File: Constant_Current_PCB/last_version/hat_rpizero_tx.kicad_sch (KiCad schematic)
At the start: 25 parts, among them SW1 MK-11C04-G013, SW2 Conn_01x04, U4 TLV75533PDBVR

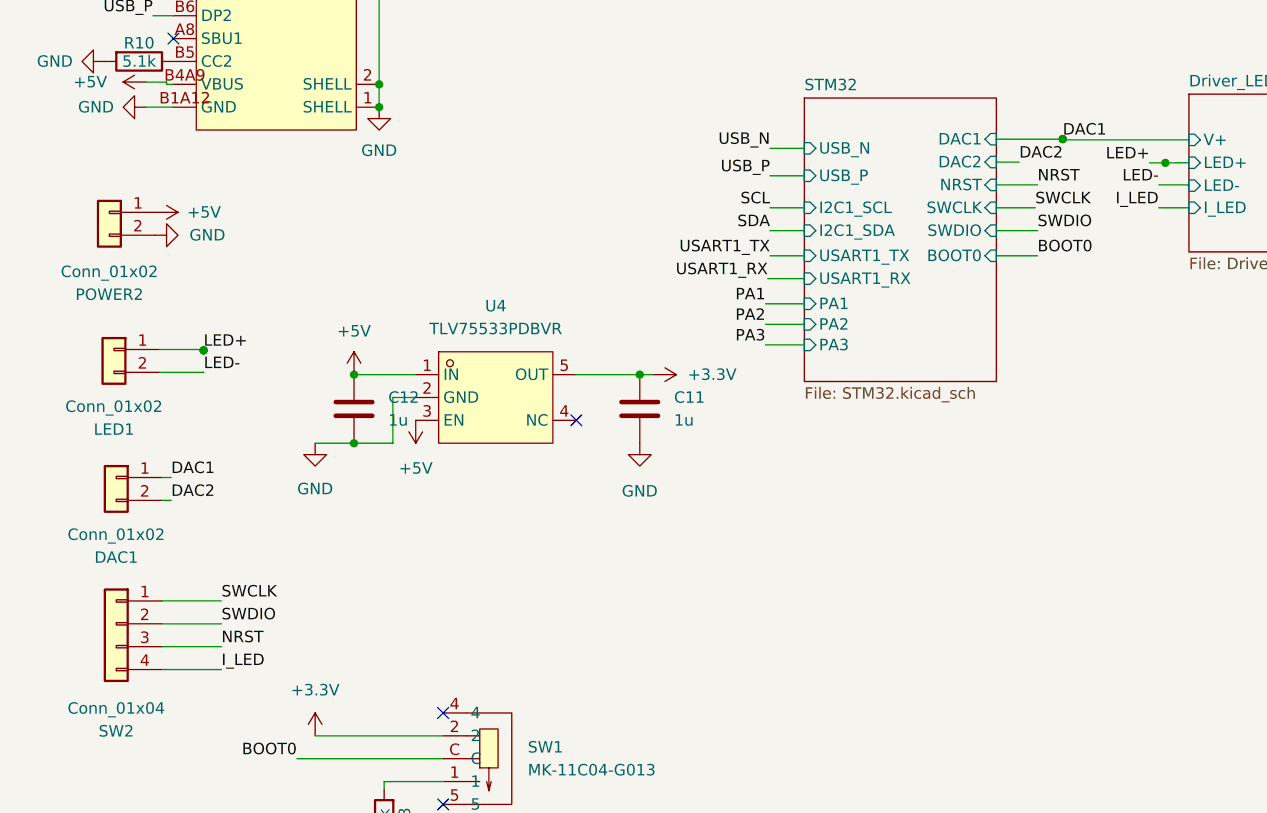
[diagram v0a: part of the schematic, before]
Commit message: fixed NRST
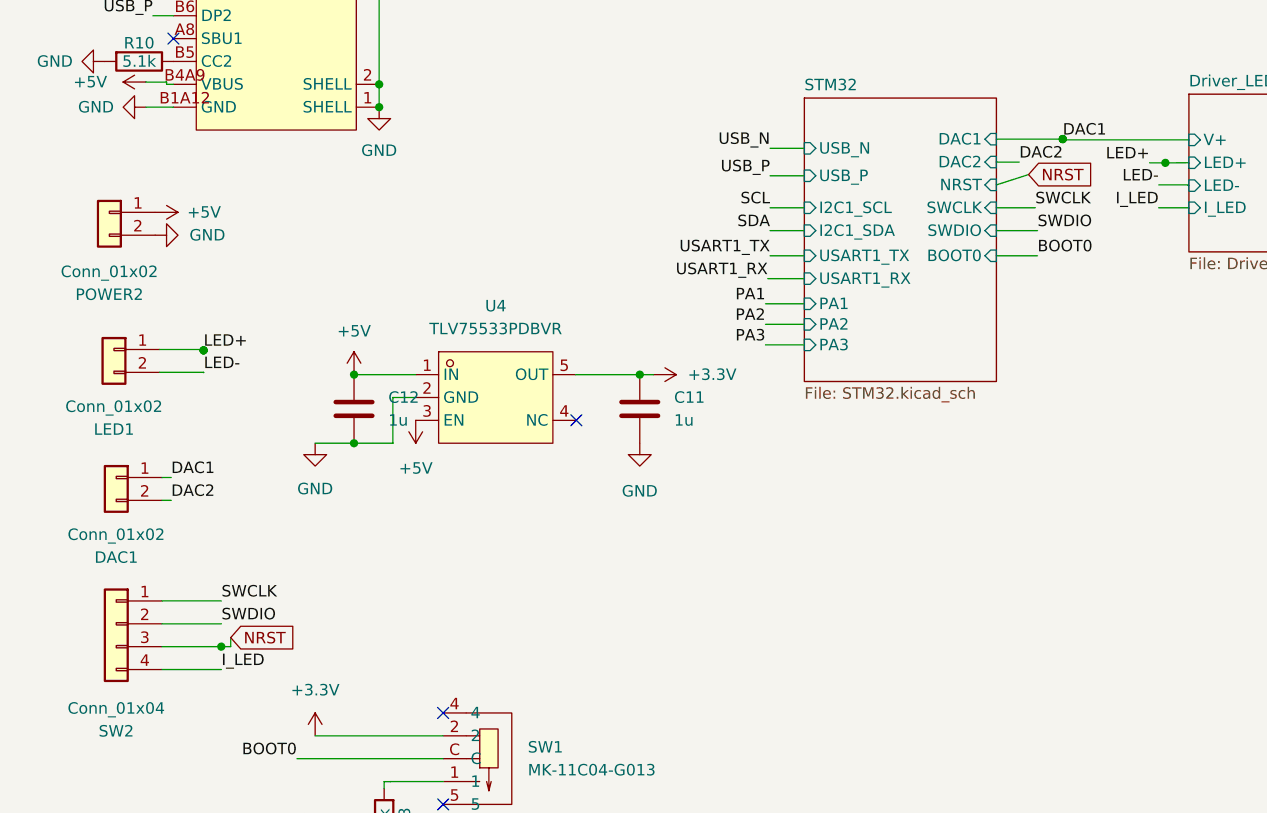
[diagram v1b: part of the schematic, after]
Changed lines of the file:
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@@
+	)
+	(junction
+		(at 36.05 111.5)
+		(diameter 0)
+		(color 0 0 0 0)
 	)
 	(junction
@@
 	(wire
 		(pts
+			(xy 37.1 110.5) (xy 37.1 111.5)
+		)
+		(stroke
+			(width 0)
+			(type default)
+		)
+	)
+	(wire
+		(pts
 			(xy 96.774 70.612) (xy 100.838 70.612)
 		)
@@
 	(wire
 		(pts
+			(xy 36.05 111.5) (xy 29.464 111.506)
+		)
+		(stroke
+			(width 0)
+			(type default)
+		)
+	)
+	(wire
+		(pts
+			(xy 125.75 59.05) (xy 122.174 60.198)
+		)
+		(stroke
+			(width 0)
+			(type default)
+		)
+	)
+	(wire
+		(pts
 			(xy 53.594 23.622) (xy 53.594 26.162)
 		)
@@
 	(wire
 		(pts
-			(xy 36.068 111.506) (xy 29.464 111.506)
+			(xy 36.068 111.506) (xy 36.05 111.5)
 		)
 		(stroke
@@
 	(wire
 		(pts
-			(xy 126.746 60.198) (xy 122.174 60.198)
-		)
-		(stroke
-			(width 0)
-			(type default)
-		)
-	)
-	(wire
-		(pts
 			(xy 119.126 164.338) (xy 119.126 162.56)
 		)
@@
 		(pts
 			(xy 34.0855 78.5841) (xy 34.0858 78.5841)
+		)
+		(stroke
+			(width 0)
+			(type default)
+		)
+	)
+	(wire
+		(pts
+			(xy 37.1 111.5) (xy 36.05 111.5)
 		)
 		(stroke
@@
 		)
 	)
-	(label "NRST"
-		(at 126.746 60.198 0)
-		(effects
-			(font
-				(size 1.27 1.27)
-			)
-			(justify left bottom)
-		)
-	)
 	(label "LED-"
 		(at 34.1 81.05 0)
@@
 		)
 	)
-	(label "NRST"
-		(at 36.068 111.506 0)
-		(effects
-			(font
-				(size 1.27 1.27)
-			)
-			(justify left bottom)
-		)
-	)
+	(global_label "NRST"
+		(shape input)
+		(at 37.1 110.5 0)
+		(fields_autoplaced yes)
+		(effects
+			(font
+				(size 1.27 1.27)
+			)
+			(justify left)
+		)
+		(property "Intersheetrefs" "${INTERSHEET_REFS}"
+			(at 44.8628 110.5 0)
+			(effects
+				(font
+					(size 1.27 1.27)
+				)
+				(justify left)
+				(hide yes)
+			)
+		)
+	)
+	(global_label "NRST"
+		(shape input)
+		(at 125.75 59.05 0)
+		(fields_autoplaced yes)
+		(effects
+			(font
+				(size 1.27 1.27)
+			)
+			(justify left)
+		)
+		(property "Intersheetrefs" "${INTERSHEET_REFS}"
+			(at 133.5128 59.05 0)
+			(effects
+				(font
+					(size 1.27 1.27)
+				)
+				(justify left)
+				(hide yes)
+			)
+		)
+	)
